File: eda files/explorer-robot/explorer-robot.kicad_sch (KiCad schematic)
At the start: 6 parts, among them U1 RP2354B

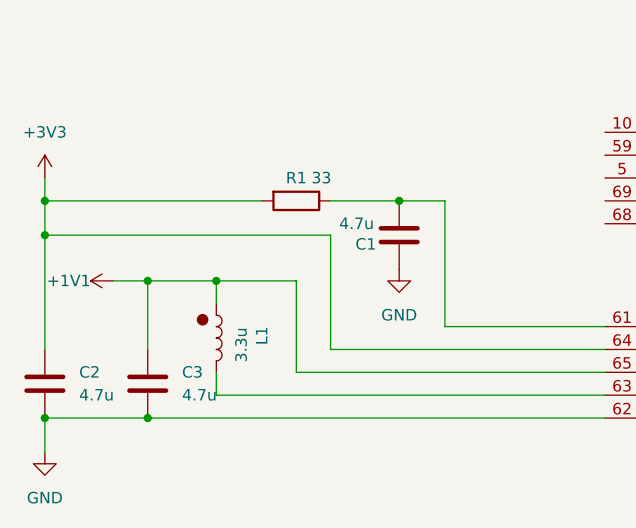
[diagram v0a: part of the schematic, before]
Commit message: Update schematic footprints and reposition power filter network
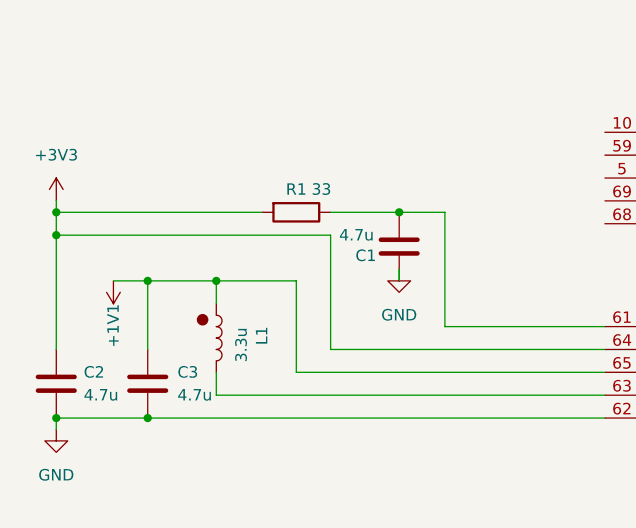
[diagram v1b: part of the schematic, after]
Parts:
- L1: footprint Inductor_SMD:L_0805_2012Metric -> rp235xb:abracon_aota-b201610s3r3-101-t
- R1: footprint Package_QFP:PQFP-160_28x28mm_P0.65mm -> Resistor_SMD:R_01005_0402Metric
- U1: footprint Package_DFN_QFN:QFN-80-1EP_10x10mm_P0.4mm_EP3.4x3.4mm -> rp235xb:rpi_rp2350b_vias
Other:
- moved on the sheet: C1, C2, R1

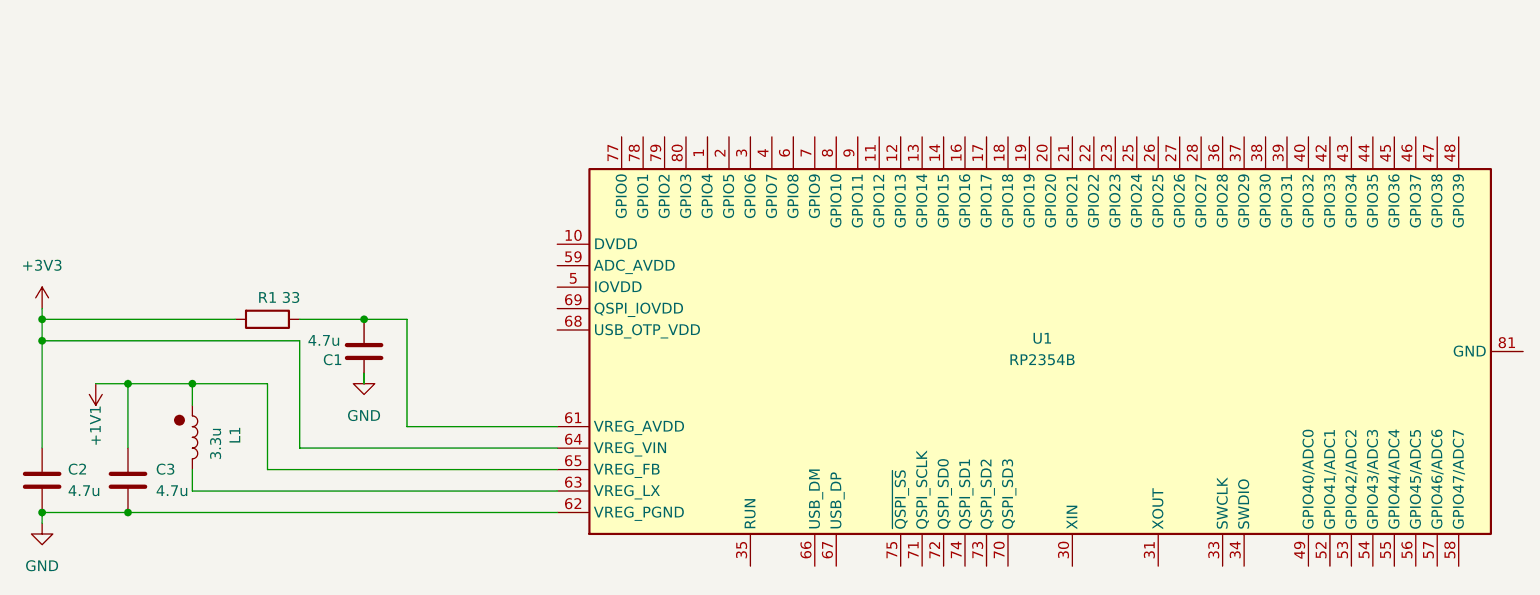
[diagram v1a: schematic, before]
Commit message: Add ICM-20948 schematic and document power design
The IMU needs a dedicated 1.8 V rail since its VDDIO is 1.8 V
only, unlike the MPU-9250. Add ADR 0017 recording the power and
level-shifting topology.

Split the RP2354B into its own schematic sheet and place the
ICM-20948 with the TXB0108 level shifter on a separate sheet.
Generate the initial PCB layout and bump the revision to v.0.1.
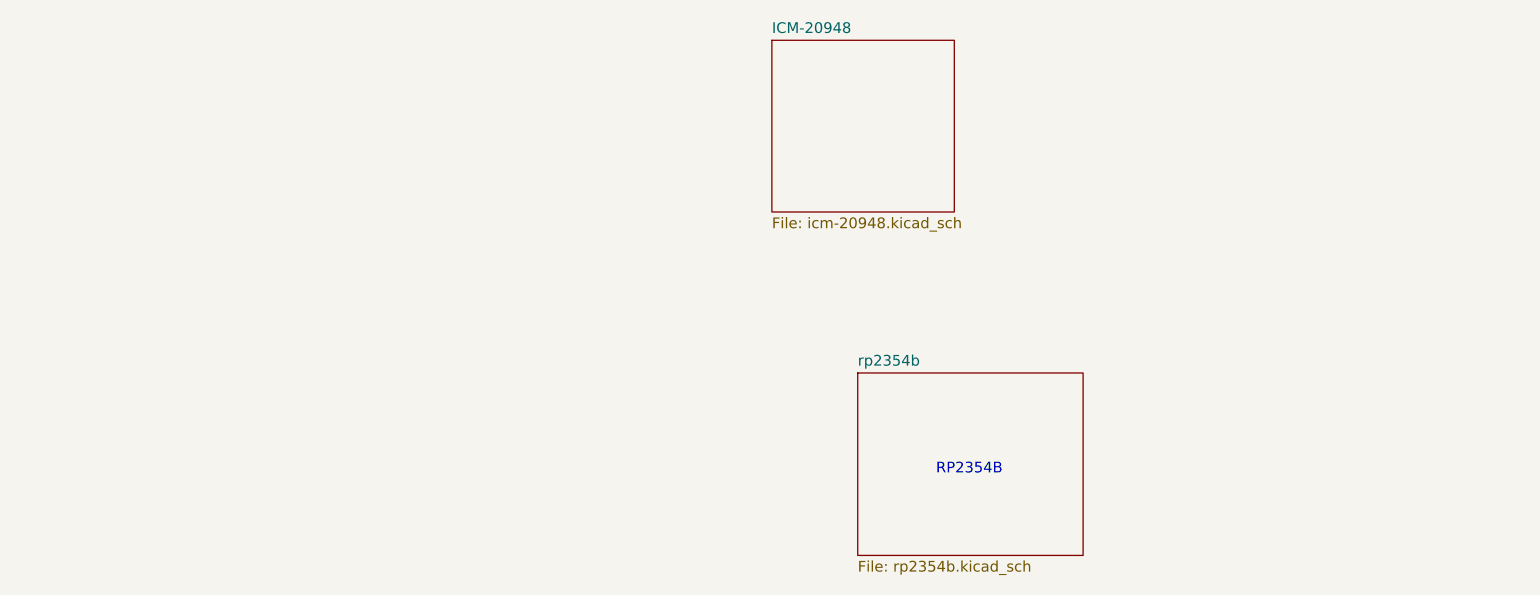
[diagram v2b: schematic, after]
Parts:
- removed C1, C2, C3: 4.7u, Capacitor_SMD:C_0402_1005Metric, symbol Device:C
- removed L1: 3.3u, rp235xb:abracon_aota-b201610s3r3-101-t, symbol Device:L
- removed R1: 33, Resistor_SMD:R_01005_0402Metric, symbol Device:R
- removed U1: RP2354B, rp235xb:rpi_rp2350b_vias, symbol MCU_RaspberryPi:RP2354B
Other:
- added sheet ICM-20948 (icm-20948.kicad_sch)
- added sheet rp2354b (rp2354b.kicad_sch)
- note added: "RP2354B"
- company: (none) -> 1-rafael-1

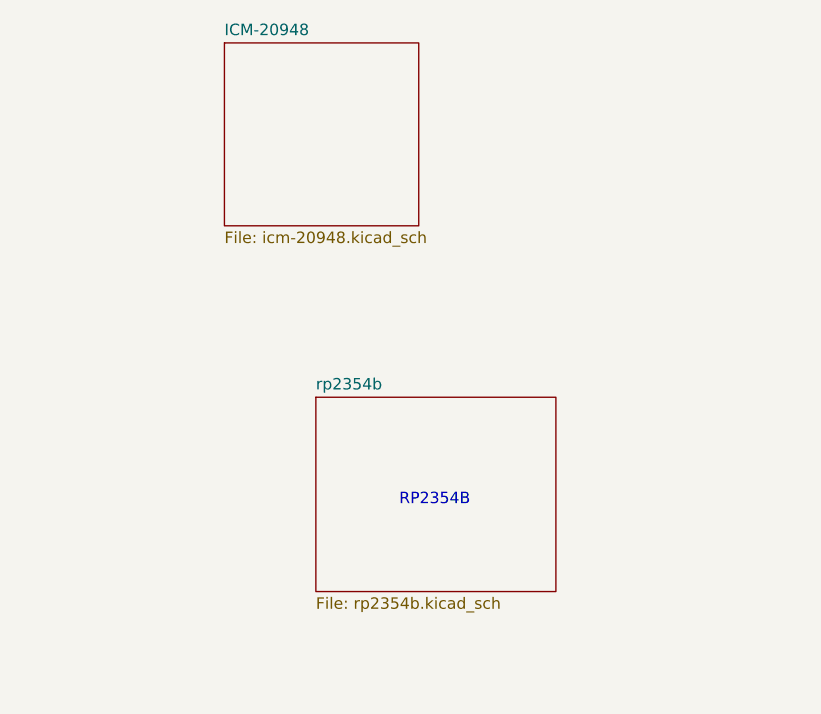
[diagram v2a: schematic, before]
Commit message: finish schematic for ICM-20948; requiring changes to pin assignment
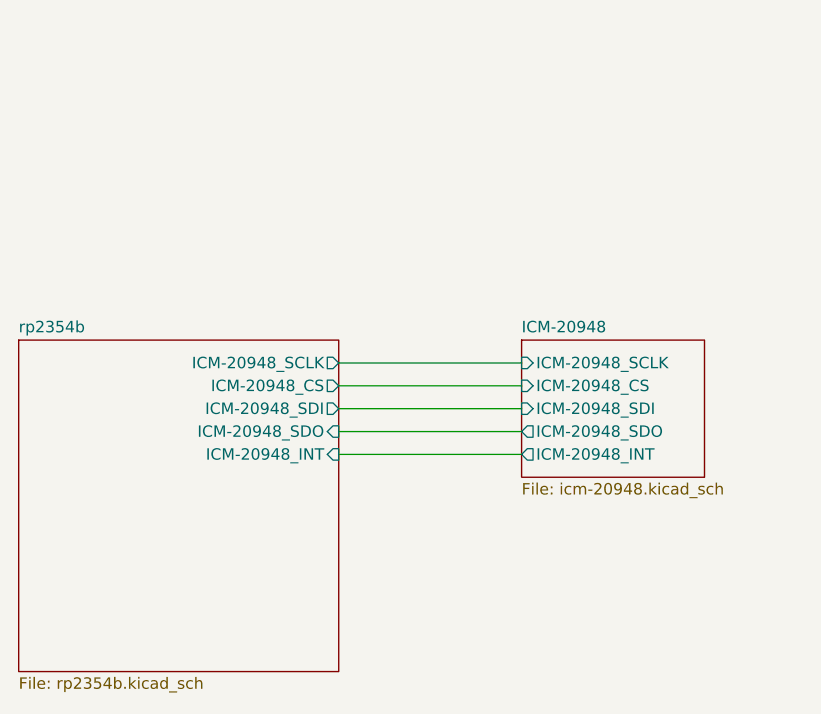
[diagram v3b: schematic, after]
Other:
- sheet ICM-20948 ports: added ICM-20948_CS, ICM-20948_INT, ICM-20948_SCLK, ICM-20948_SDI, ICM-20948_SDO; removed none
- sheet rp2354b ports: added ICM-20948_CS, ICM-20948_INT, ICM-20948_SCLK, ICM-20948_SDI, ICM-20948_SDO; removed none
- note removed: "RP2354B"
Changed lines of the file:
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@@
 		(company "1-rafael-1")
 	)
-	(text "RP2354B"
-		(exclude_from_sim no)
-		(at 151.638 105.41 0)
-		(effects
-			(font
-				(size 1.27 1.27)
-			)
+	(wire
+		(pts
+			(xy 140.97 97.79) (xy 161.29 97.79)
+		)
+		(stroke
+			(width 0)
+			(type default)
+		)
+	)
+	(wire
+		(pts
+			(xy 140.97 92.71) (xy 161.29 92.71)
+		)
+		(stroke
+			(width 0)
+			(type default)
+		)
+	)
+	(wire
+		(pts
+			(xy 140.97 90.17) (xy 161.29 90.17)
+		)
+		(stroke
+			(width 0)
+			(type default)
+		)
+	)
+	(wire
+		(pts
+			(xy 140.97 95.25) (xy 161.29 95.25)
+		)
+		(stroke
+			(width 0)
+			(type default)
+		)
+	)
+	(wire
+		(pts
+			(xy 140.97 100.33) (xy 161.29 100.33)
+		)
+		(stroke
+			(width 0)
+			(type default)
 		)
 	)
 	(sheet
-		(at 138.43 93.98)
-		(size 26.67 21.59)
+		(at 105.41 87.63)
+		(size 35.56 36.83)
 		(exclude_from_sim no)
 		(in_bom yes)
@@
 		)
 		(property "Sheetname" "rp2354b"
-			(at 138.43 93.2684 0)
+			(at 105.41 86.9184 0)
 			(show_name no)
 			(do_not_autoplace no)
@@
 		)
 		(property "Sheetfile" "rp2354b.kicad_sch"
-			(at 138.43 116.1546 0)
+			(at 105.41 125.0446 0)
 			(show_name no)
 			(do_not_autoplace no)
@@
 				)
 				(justify left top)
+			)
+		)
+		(pin "ICM-20948_INT" input
+			(at 140.97 100.33 0)
+			(effects
+				(font
+					(size 1.27 1.27)
+				)
+				(justify right)
+			)
+		)
+		(pin "ICM-20948_SDO" input
+			(at 140.97 97.79 0)
+			(effects
+				(font
+					(size 1.27 1.27)
+				)
+				(justify right)
+			)
+		)
+		(pin "ICM-20948_CS" output
+			(at 140.97 92.71 0)
+			(effects
+				(font
+					(size 1.27 1.27)
+				)
+				(justify right)
+			)
+		)
+		(pin "ICM-20948_SCLK" output
+			(at 140.97 90.17 0)
+			(effects
+				(font
+					(size 1.27 1.27)
+				)
+				(justify right)
+			)
+		)
+		(pin "ICM-20948_SDI" output
+			(at 140.97 95.25 0)
+			(effects
+				(font
+					(size 1.27 1.27)
+				)
+				(justify right)
 			)
 		)
@@
 	)
 	(sheet
-		(at 128.27 54.61)
-		(size 21.59 20.32)
+		(at 161.29 87.63)
+		(size 20.32 15.24)
 		(exclude_from_sim no)
 		(in_bom yes)
@@
 		)
 		(property "Sheetname" "ICM-20948"
-			(at 128.27 53.8984 0)
+			(at 161.29 86.9184 0)
 			(show_name no)
 			(do_not_autoplace no)
@@
 		)
 		(property "Sheetfile" "icm-20948.kicad_sch"
-			(at 128.27 75.5146 0)
+			(at 161.29 103.4546 0)
 			(show_name no)
 			(do_not_autoplace no)
@@
 			)
 		)
+		(pin "ICM-20948_SDO" output
+			(at 161.29 97.79 180)
+			(effects
+				(font
+					(size 1.27 1.27)
+				)
+				(justify left)
+			)
+		)
+		(pin "ICM-20948_CS" input
+			(at 161.29 92.71 180)
+			(effects
+				(font
+					(size 1.27 1.27)
+				)
+				(justify left)
+			)
+		)
+		(pin "ICM-20948_SCLK" input
+			(at 161.29 90.17 180)
+			(effects
+				(font
+					(size 1.27 1.27)
+				)
+				(justify left)
+			)
+		)
+		(pin "ICM-20948_SDI" input
+			(at 161.29 95.25 180)
+			(effects
+				(font
+					(size 1.27 1.27)
+				)
+				(justify left)
+			)
+		)
+		(pin "ICM-20948_INT" output
+			(at 161.29 100.33 180)
+			(effects
+				(font
+					(size 1.27 1.27)
+				)
+				(justify left)
+			)
+		)

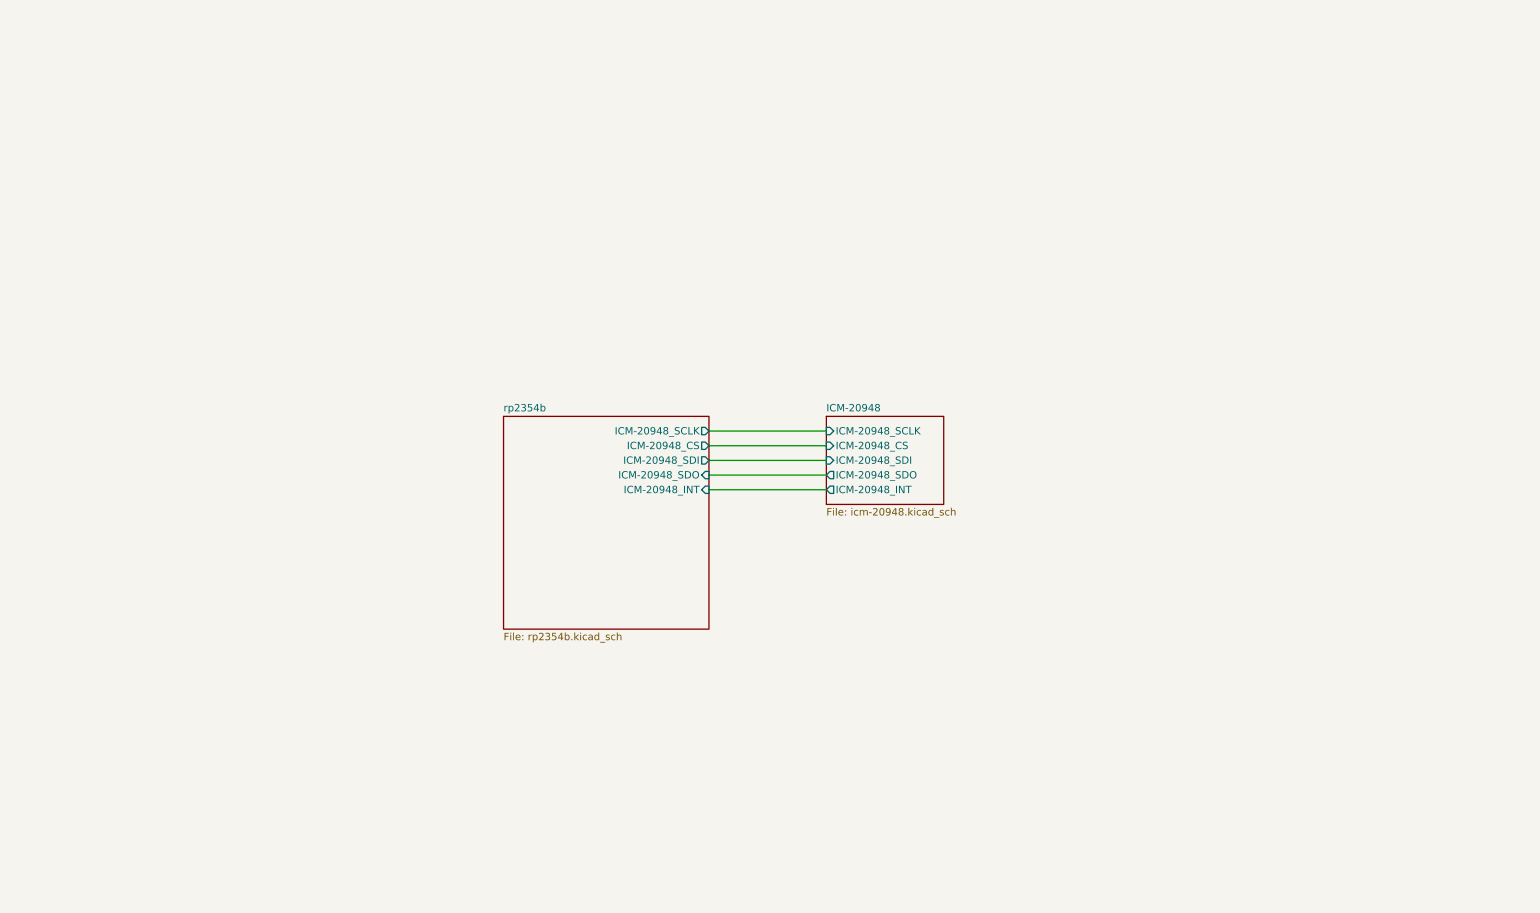
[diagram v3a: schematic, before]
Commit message: Split power and motor driver into dedicated schematic sheets
Add ADRs 0018–0020 covering ground topology, battery rail and
connector protection decisions. Move battery, 5 V buck and test points
to a new power_and_batt sheet, and the TB6612FNG with motor connectors
to a new tb6612fng sheet.

Collapse the single ground net at the TB6612FNG, add the three-tier VM
decoupling stack and bidirectional TVS clamps on the motor pairs and VM.
Switch the 5 V rail to a TPS5430DDAR with a 220 µF/25 V polymer bulk
shared across the battery, VM and 5 V rails. Fix the ICM-20948 regulator
symbol to AMS1117-1.8.
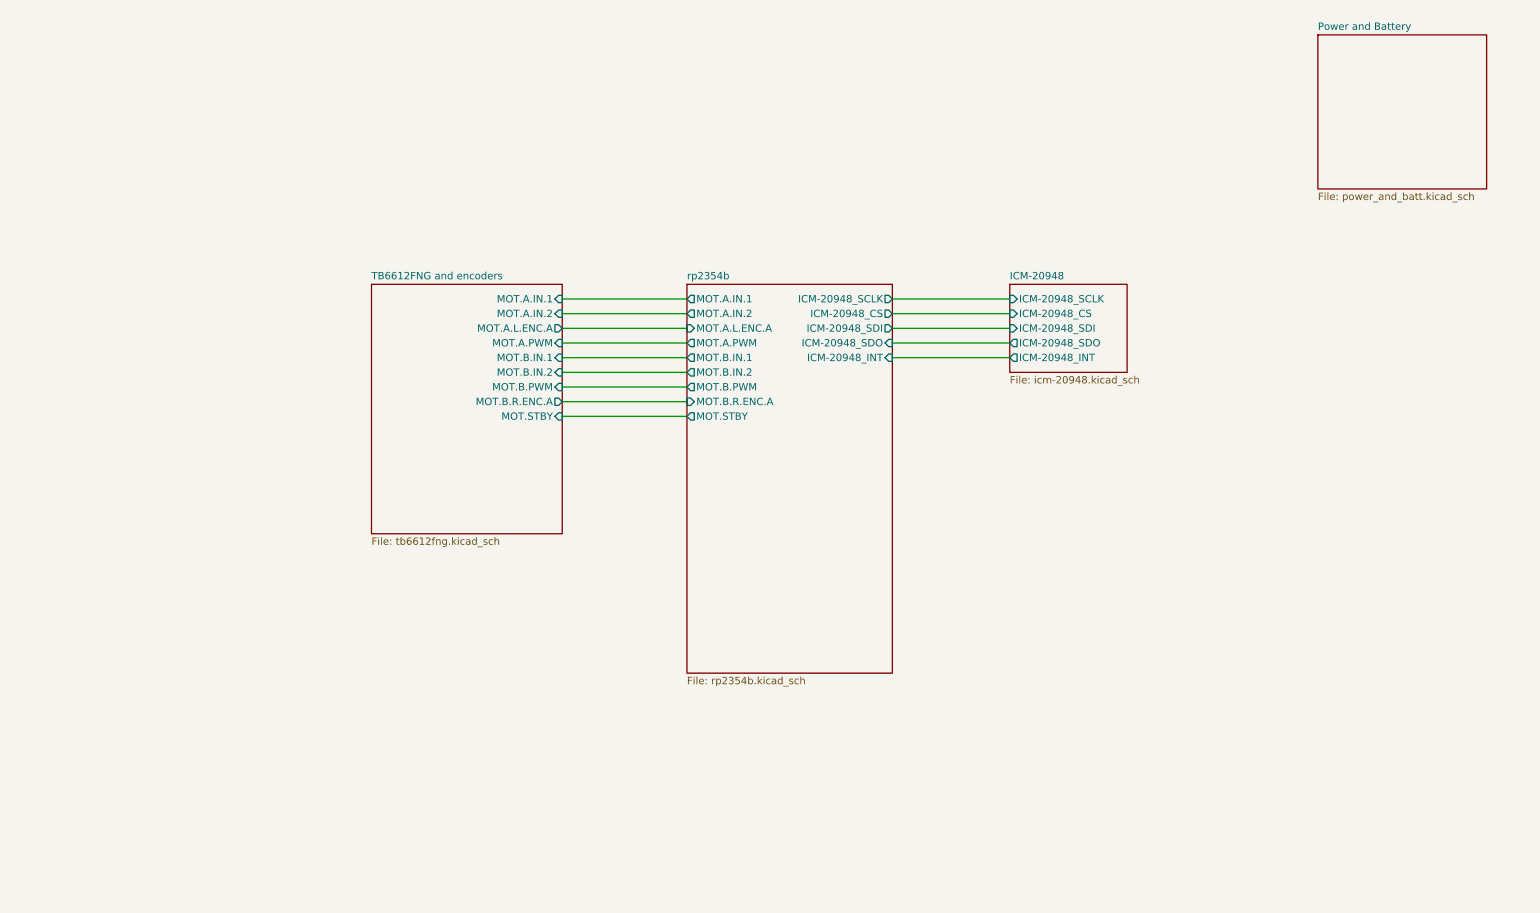
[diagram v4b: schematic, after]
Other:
- added sheet Power and Battery (power_and_batt.kicad_sch)
- added sheet TB6612FNG and encoders (tb6612fng.kicad_sch)
- sheet rp2354b ports: added MOT.A.IN.1, MOT.A.IN.2, MOT.A.L.ENC.A, MOT.A.PWM, MOT.B.IN.1, MOT.B.IN.2, MOT.B.PWM, MOT.B.R.ENC.A, MOT.STBY; removed none
